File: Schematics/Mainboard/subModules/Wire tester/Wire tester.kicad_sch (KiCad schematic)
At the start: 7 parts, among them J1 Input, Q1 SS8050

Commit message: added prelim wire tester
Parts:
- removed J1: Input, Connector_PinSocket_2.54mm:PinSocket_1x04_P2.54mm_Vertical, symbol Connector:Conn_01x04_Female
- added TP3: 3.3V Wire TP, TestPoint:TestPoint_Keystone_5015_Micro-Minature, symbol Connector:TestPoint
- added TP4: GND Wire TP, TestPoint:TestPoint_Keystone_5015_Micro-Minature, symbol Connector:TestPoint
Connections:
- net +3V3: now also TP3.1
- net GND: now also TP4.1
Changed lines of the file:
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@@
     (company "Alex Carter")
   )
-  (junction (at 48.895 52.705) (diameter 1.016) (color 0 0 0 0))
-  (junction (at 48.895 60.325) (diameter 1.016) (color 0 0 0 0))
-  (wire (pts (xy 47.625 52.705) (xy 48.895 52.705))
-    (stroke (width 0) (type solid) (color 0 0 0 0))
-  )
-  (wire (pts (xy 47.625 55.245) (xy 48.895 55.245))
-    (stroke (width 0) (type solid) (color 0 0 0 0))
-  )
-  (wire (pts (xy 47.625 57.785) (xy 48.895 57.785))
-    (stroke (width 0) (type solid) (color 0 0 0 0))
-  )
-  (wire (pts (xy 47.625 60.325) (xy 48.895 60.325))
-    (stroke (width 0) (type solid) (color 0 0 0 0))
-  )
-  (wire (pts (xy 48.895 52.705) (xy 50.165 52.705))
-    (stroke (width 0) (type solid) (color 0 0 0 0))
-  )
-  (wire (pts (xy 48.895 55.245) (xy 48.895 52.705))
-    (stroke (width 0) (type solid) (color 0 0 0 0))
-  )
-  (wire (pts (xy 48.895 57.785) (xy 48.895 60.325))
-    (stroke (width 0) (type solid) (color 0 0 0 0))
-  )
-  (wire (pts (xy 48.895 60.325) (xy 50.165 60.325))
+  (wire (pts (xy 47.625 75.565) (xy 48.895 75.565))
+    (stroke (width 0) (type solid) (color 0 0 0 0))
+  )
+  (wire (pts (xy 48.895 83.185) (xy 47.625 83.185))
     (stroke (width 0) (type solid) (color 0 0 0 0))
   )
@@
     (stroke (width 0) (type solid) (color 0 0 0 0))
   )
-  (symbol (lib_id "power:+3.3V") (at 50.165 52.705 270) (unit 1)
-    (in_bom yes) (on_board yes) (fields_autoplaced)
-    (property "Reference" "#PWR0105" (id 0) (at 46.355 52.705 0)
-      (effects (font (size 1.27 1.27)) hide)
-    )
-    (property "Value" "+3.3V" (id 1) (at 53.3401 53.184 90)
-      (effects (font (size 1.27 1.27)) (justify left))
-    )
-    (property "Footprint" "" (id 2) (at 50.165 52.705 0)
-      (effects (font (size 1.27 1.27)) hide)
-    )
-    (property "Datasheet" "" (id 3) (at 50.165 52.705 0)
+  (symbol (lib_id "power:+3.3V") (at 48.895 75.565 270) (unit 1)
+    (in_bom yes) (on_board yes) (fields_autoplaced)
+    (property "Reference" "#PWR0105" (id 0) (at 45.085 75.565 0)
+      (effects (font (size 1.27 1.27)) hide)
+    )
+    (property "Value" "+3.3V" (id 1) (at 52.0701 76.044 90)
+      (effects (font (size 1.27 1.27)) (justify left))
+    )
+    (property "Footprint" "" (id 2) (at 48.895 75.565 0)
+      (effects (font (size 1.27 1.27)) hide)
+    )
+    (property "Datasheet" "" (id 3) (at 48.895 75.565 0)
       (effects (font (size 1.27 1.27)) hide)
     )
@@
     )
     (property "Datasheet" "" (id 3) (at 111.76 46.99 0)
+      (effects (font (size 1.27 1.27)) hide)
+    )
+    (pin "1")
+  )
+  (symbol (lib_id "Connector:TestPoint") (at 47.625 75.565 90) (mirror x) (unit 1)
+    (in_bom yes) (on_board yes) (fields_autoplaced)
+    (property "Reference" "TP3" (id 0) (at 42.9259 74.6565 90)
+      (effects (font (size 1.27 1.27)) (justify left))
+    )
+    (property "Value" "3.3V Wire TP" (id 1) (at 42.9259 77.4316 90)
+      (effects (font (size 1.27 1.27)) (justify left))
+    )
+    (property "Footprint" "TestPoint:TestPoint_Keystone_5015_Micro-Minature" (id 2) (at 47.625 80.645 0)
+      (effects (font (size 1.27 1.27)) hide)
+    )
+    (property "Datasheet" "~" (id 3) (at 47.625 80.645 0)
+      (effects (font (size 1.27 1.27)) hide)
+    )
+    (pin "1")
+  )
+  (symbol (lib_id "Connector:TestPoint") (at 47.625 83.185 90) (mirror x) (unit 1)
+    (in_bom yes) (on_board yes) (fields_autoplaced)
+    (property "Reference" "TP4" (id 0) (at 42.9259 82.2765 90)
+      (effects (font (size 1.27 1.27)) (justify left))
+    )
+    (property "Value" "GND Wire TP" (id 1) (at 42.9259 85.0516 90)
+      (effects (font (size 1.27 1.27)) (justify left))
+    )
+    (property "Footprint" "TestPoint:TestPoint_Keystone_5015_Micro-Minature" (id 2) (at 47.625 88.265 0)
+      (effects (font (size 1.27 1.27)) hide)
+    )
+    (property "Datasheet" "~" (id 3) (at 47.625 88.265 0)
       (effects (font (size 1.27 1.27)) hide)
     )
@@
     (pin "1")
   )
-  (symbol (lib_id "power:GND") (at 50.165 60.325 90) (mirror x) (unit 1)
-    (in_bom yes) (on_board yes) (fields_autoplaced)
-    (property "Reference" "#PWR0104" (id 0) (at 56.515 60.325 0)
-      (effects (font (size 1.27 1.27)) hide)
-    )
-    (property "Value" "GND" (id 1) (at 53.3401 60.804 90)
-      (effects (font (size 1.27 1.27)) (justify right))
-    )
-    (property "Footprint" "" (id 2) (at 50.165 60.325 0)
-      (effects (font (size 1.27 1.27)) hide)
-    )
-    (property "Datasheet" "" (id 3) (at 50.165 60.325 0)
+  (symbol (lib_id "power:GND") (at 48.895 83.185 90) (mirror x) (unit 1)
+    (in_bom yes) (on_board yes) (fields_autoplaced)
+    (property "Reference" "#PWR0104" (id 0) (at 55.245 83.185 0)
+      (effects (font (size 1.27 1.27)) hide)
+    )
+    (property "Value" "GND" (id 1) (at 52.0701 83.664 90)
+      (effects (font (size 1.27 1.27)) (justify right))
+    )
+    (property "Footprint" "" (id 2) (at 48.895 83.185 0)
+      (effects (font (size 1.27 1.27)) hide)
+    )
+    (property "Datasheet" "" (id 3) (at 48.895 83.185 0)
       (effects (font (size 1.27 1.27)) hide)
     )
@@
     (pin "2")
   )
-  (symbol (lib_id "Connector:Conn_01x04_Female") (at 42.545 55.245 0) (mirror y) (unit 1)
-    (in_bom yes) (on_board yes) (fields_autoplaced)
-    (property "Reference" "J1" (id 0) (at 45.2374 48.2812 0))
-    (property "Value" "Input" (id 1) (at 45.2374 51.0563 0))
-    (property "Footprint" "Connector_PinSocket_2.54mm:PinSocket_1x04_P2.54mm_Vertical" (id 2) (at 42.545 55.245 0)
-      (effects (font (size 1.27 1.27)) hide)
-    )
-    (property "Datasheet" "~" (id 3) (at 42.545 55.245 0)
-      (effects (font (size 1.27 1.27)) hide)
-    )
-    (pin "1")
-    (pin "2")
-    (pin "3")
-    (pin "4")
-  )
   (symbol (lib_id "Transistor_BJT:2N2219") (at 109.22 66.04 0) (unit 1)
     (in_bom yes) (on_board yes) (fields_autoplaced)
@@
       (reference "#PWR0103") (unit 1) (value "GND") (footprint "")
     )
-    (path "/ec4a6d38-f933-45b9-a174-c4b039a33be7"
+    (path "/bb6b585f-830f-48b0-8f3c-7a57549c6043"
       (reference "#PWR0104") (unit 1) (value "GND") (footprint "")
     )
-    (path "/91c5b4ba-4f16-46d4-bdf2-c67fbeb42dff"
+    (path "/75890350-b903-4047-a977-f44fca4842a6"
       (reference "#PWR0105") (unit 1) (value "+3.3V") (footprint "")
     )
@@
       (reference "D1") (unit 1) (value "Red 5mm") (footprint "LED_THT:LED_D5.0mm")
     )
-    (path "/a22a4c3d-1755-4430-9625-5c07a0ea1276"
-      (reference "J1") (unit 1) (value "Input") (footprint "Connector_PinSocket_2.54mm:PinSocket_1x04_P2.54mm_Vertical")
-    )
     (path "/10a5e36d-268b-4750-8292-4b7026879dc4"
       (reference "Q1") (unit 1) (value "SS8050") (footprint "Package_TO_SOT_SMD:SOT-23")
@@
       (reference "TP2") (unit 1) (value "Wire a") (footprint "TestPoint:TestPoint_Pad_4.0x4.0mm")
     )
-  )
+    (path "/5705f52f-b7b9-4c6a-bb87-53a8e1046886"
+      (reference "TP3") (unit 1) (value "3.3V Wire TP") (footprint "TestPoint:TestPoint_Keystone_5015_Micro-Minature")
+    )
+    (path "/1b9ba5c0-828f-4f45-9c63-805cf2bff41f"
+      (reference "TP4") (unit 1) (value "GND Wire TP") (footprint "TestPoint:TestPoint_Keystone_5015_Micro-Minature")
+    )
+  )

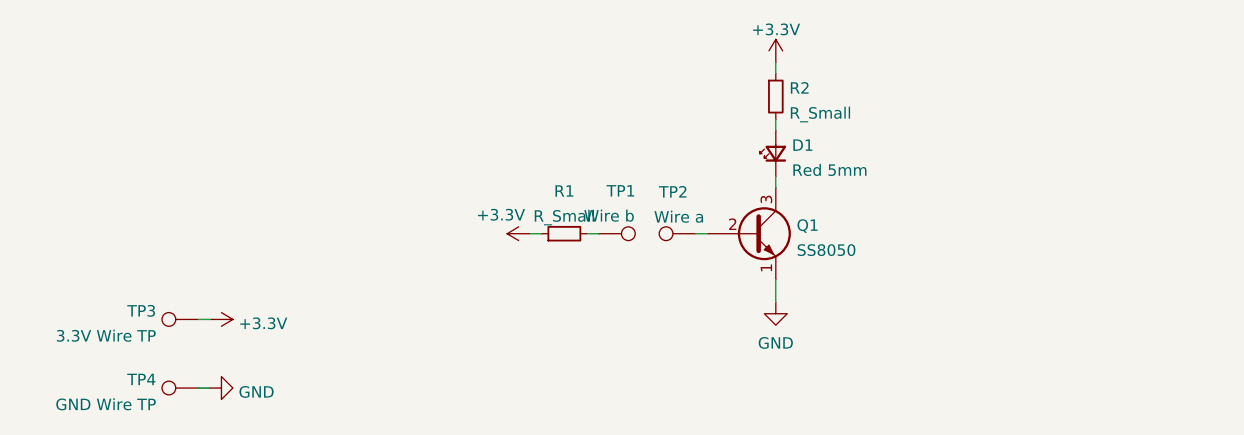
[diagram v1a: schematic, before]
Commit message: Added proper text to wire tester board
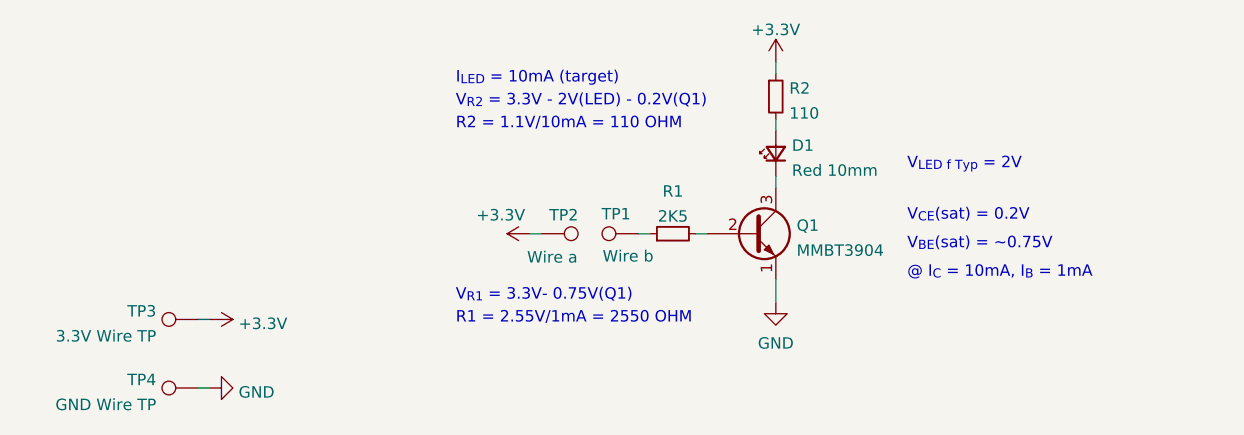
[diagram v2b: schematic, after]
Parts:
- D1: value Red 5mm -> Red 10mm
- Q1: value SS8050 -> MMBT3904
- R1: value R_Small -> 2K5
- R2: value R_Small -> 110
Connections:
- net +3V3: now also TP2.1; no longer R1.1
- net at Q1.2 (B): now also R1.2; no longer TP2.1
- net at TP1.1: now also R1.1; no longer R1.2
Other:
- note added: "@ I_{C} = 10mA, I_{B} = 1mA"
- note added: "I_{LED} = 10mA (target)"
- note added: "R1 = 2.55V/1mA = 2550 OHM"
- note added: "R2 = 1.1V/10mA = 110 OHM"
- note added: "V_{BE}(sat) = ~0.75V"
- note added: "V_{CE}(sat) = 0.2V"
- note added: "V_{LED f Typ} = 2V"
- note added: "V_{R1} = 3.3V- 0.75V(Q1)"
- note added: "V_{R2} = 3.3V - 2V(LED) - 0.2V(Q1)"
- moved on the sheet: R1, TP1, TP2
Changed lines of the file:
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@@
     (stroke (width 0) (type solid) (color 0 0 0 0))
   )
-  (wire (pts (xy 90.805 66.04) (xy 92.075 66.04))
+  (wire (pts (xy 96.52 66.04) (xy 97.79 66.04))
     (stroke (width 0) (type solid) (color 0 0 0 0))
   )
@@
   (wire (pts (xy 111.76 71.12) (xy 111.76 73.66))
     (stroke (width 0) (type solid) (color 0 0 0 0))
+  )
+  (text "I_{LED} = 10mA (target)" (at 76.2 49.53 0)
+    (effects (font (size 1.27 1.27)) (justify left bottom))
+  )
+  (text "V_{R2} = 3.3V - 2V(LED) - 0.2V(Q1)" (at 76.2 52.07 0)
+    (effects (font (size 1.27 1.27)) (justify left bottom))
+  )
+  (text "R2 = 1.1V/10mA = 110 OHM" (at 76.2 54.61 0)
+    (effects (font (size 1.27 1.27)) (justify left bottom))
+  )
+  (text "V_{R1} = 3.3V- 0.75V(Q1)" (at 76.2 73.66 0)
+    (effects (font (size 1.27 1.27)) (justify left bottom))
+  )
+  (text "R1 = 2.55V/1mA = 2550 OHM" (at 76.2 76.2 0)
+    (effects (font (size 1.27 1.27)) (justify left bottom))
+  )
+  (text "V_{LED f Typ} = 2V " (at 126.365 59.055 0)
+    (effects (font (size 1.27 1.27)) (justify left bottom))
+  )
+  (text "V_{CE}(sat) = 0.2V" (at 126.365 64.77 0)
+    (effects (font (size 1.27 1.27)) (justify left bottom))
+  )
+  (text "V_{BE}(sat) = ~0.75V" (at 126.365 67.945 0)
+    (effects (font (size 1.27 1.27)) (justify left bottom))
+  )
+  (text "@ I_{C} = 10mA, I_{B} = 1mA" (at 126.365 71.12 0)
+    (effects (font (size 1.27 1.27)) (justify left bottom))
   )
   (symbol (lib_id "power:+3.3V") (at 48.895 75.565 270) (unit 1)
@@
     (pin "1")
   )
-  (symbol (lib_id "Connector:TestPoint") (at 92.075 66.04 270) (mirror x) (unit 1)
+  (symbol (lib_id "Connector:TestPoint") (at 85.725 66.04 270) (mirror x) (unit 1)
     (in_bom yes) (on_board yes)
-    (property "Reference" "TP1" (id 0) (at 92.9641 61.3215 90)
-      (effects (font (size 1.27 1.27)) (justify left))
-    )
-    (property "Value" "Wire b" (id 1) (at 90.4241 64.0966 90)
-      (effects (font (size 1.27 1.27)) (justify left))
-    )
-    (property "Footprint" "TestPoint:TestPoint_Pad_4.0x4.0mm" (id 2) (at 92.075 60.96 0)
-      (effects (font (size 1.27 1.27)) hide)
-    )
-    (property "Datasheet" "~" (id 3) (at 92.075 60.96 0)
-      (effects (font (size 1.27 1.27)) hide)
-    )
-    (pin "1")
-  )
-  (symbol (lib_id "Connector:TestPoint") (at 102.87 66.04 90) (unit 1)
+    (property "Reference" "TP2" (id 0) (at 88.2015 63.9784 90))
+    (property "Value" "Wire a" (id 1) (at 86.9315 68.6585 90))
+    (property "Footprint" "TestPoint:TestPoint_Pad_4.0x4.0mm" (id 2) (at 85.725 60.96 0)
+      (effects (font (size 1.27 1.27)) hide)
+    )
+    (property "Datasheet" "~" (id 3) (at 85.725 60.96 0)
+      (effects (font (size 1.27 1.27)) hide)
+    )
+    (pin "1")
+  )
+  (symbol (lib_id "Connector:TestPoint") (at 96.52 66.04 90) (unit 1)
     (in_bom yes) (on_board yes)
-    (property "Reference" "TP2" (id 0) (at 100.3935 61.4384 90))
-    (property "Value" "Wire a" (id 1) (at 101.0285 64.2135 90))
-    (property "Footprint" "TestPoint:TestPoint_Pad_4.0x4.0mm" (id 2) (at 102.87 60.96 0)
-      (effects (font (size 1.27 1.27)) hide)
-    )
-    (property "Datasheet" "~" (id 3) (at 102.87 60.96 0)
+    (property "Reference" "TP1" (id 0) (at 95.6309 63.8615 90)
+      (effects (font (size 1.27 1.27)) (justify left))
+    )
+    (property "Value" "Wire b" (id 1) (at 98.1709 68.5416 90)
+      (effects (font (size 1.27 1.27)) (justify left))
+    )
+    (property "Footprint" "TestPoint:TestPoint_Pad_4.0x4.0mm" (id 2) (at 96.52 60.96 0)
+      (effects (font (size 1.27 1.27)) hide)
+    )
+    (property "Datasheet" "~" (id 3) (at 96.52 60.96 0)
       (effects (font (size 1.27 1.27)) hide)
     )
@@
     (pin "1")
   )
-  (symbol (lib_id "Device:R_Small") (at 88.265 66.04 90) (unit 1)
-    (in_bom yes) (on_board yes) (fields_autoplaced)
-    (property "Reference" "R1" (id 0) (at 88.265 61.3368 90))
-    (property "Value" "R_Small" (id 1) (at 88.265 64.1119 90))
-    (property "Footprint" "Resistor_SMD:R_0603_1608Metric" (id 2) (at 88.265 66.04 0)
-      (effects (font (size 1.27 1.27)) hide)
-    )
-    (property "Datasheet" "~" (id 3) (at 88.265 66.04 0)
+  (symbol (lib_id "Device:R_Small") (at 100.33 66.04 90) (unit 1)
+    (in_bom yes) (on_board yes) (fields_autoplaced)
+    (property "Reference" "R1" (id 0) (at 100.33 61.3368 90))
+    (property "Value" "2K5" (id 1) (at 100.33 64.1119 90))
+    (property "Footprint" "Resistor_SMD:R_0603_1608Metric" (id 2) (at 100.33 66.04 0)
+      (effects (font (size 1.27 1.27)) hide)
+    )
+    (property "Datasheet" "~" (id 3) (at 100.33 66.04 0)
       (effects (font (size 1.27 1.27)) hide)
     )
@@
       (effects (font (size 1.27 1.27)) (justify left))
     )
-    (property "Value" "R_Small" (id 1) (at 113.2587 52.6666 0)
+    (property "Value" "110" (id 1) (at 113.2587 52.6666 0)
       (effects (font (size 1.27 1.27)) (justify left))
     )
@@
       (effects (font (size 1.27 1.27)) (justify right))
     )
-    (property "Value" "Red 5mm" (id 1) (at 113.5381 59.0166 90)
+    (property "Value" "Red 10mm" (id 1) (at 113.5381 59.0166 90)
       (effects (font (size 1.27 1.27)) (justify right))
     )
@@
       (effects (font (size 1.27 1.27)) (justify left))
     )
-    (property "Value" "SS8050" (id 1) (at 114.0715 67.9066 0)
+    (property "Value" "MMBT3904" (id 1) (at 114.0715 67.9066 0)
       (effects (font (size 1.27 1.27)) (justify left))
     )
@@
     )
     (path "/a76e5ec2-6eb8-4a04-bc24-41e7d9dcdb29"
-      (reference "D1") (unit 1) (value "Red 5mm") (footprint "LED_THT:LED_D5.0mm")
+      (reference "D1") (unit 1) (value "Red 10mm") (footprint "LED_THT:LED_D5.0mm")
     )
     (path "/10a5e36d-268b-4750-8292-4b7026879dc4"
-      (reference "Q1") (unit 1) (value "SS8050") (footprint "Package_TO_SOT_SMD:SOT-23")
+      (reference "Q1") (unit 1) (value "MMBT3904") (footprint "Package_TO_SOT_SMD:SOT-23")
     )
     (path "/bfdb5c3a-61a8-4113-8647-62479eff38a3"
-      (reference "R1") (unit 1) (value "R_Small") (footprint "Resistor_SMD:R_0603_1608Metric")
+      (reference "R1") (unit 1) (value "2K5") (footprint "Resistor_SMD:R_0603_1608Metric")
     )
     (path "/84a91370-705c-4c07-b0b5-74fc54223ef1"
-      (reference "R2") (unit 1) (value "R_Small") (footprint "Resistor_SMD:R_0603_1608Metric")
+      (reference "R2") (unit 1) (value "110") (footprint "Resistor_SMD:R_0603_1608Metric")
     )
     (path "/a44485a8-1578-4beb-ae24-88e898883fdd"
